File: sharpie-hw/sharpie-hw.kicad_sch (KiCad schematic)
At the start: 0 parts

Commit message: sharpie-hw prototype 1: complete
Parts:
- added H1, H2, H3, H4: MountingHole, symbol Mechanical:MountingHole
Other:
- sheet Power renamed Power_Display
- removed sheet Display

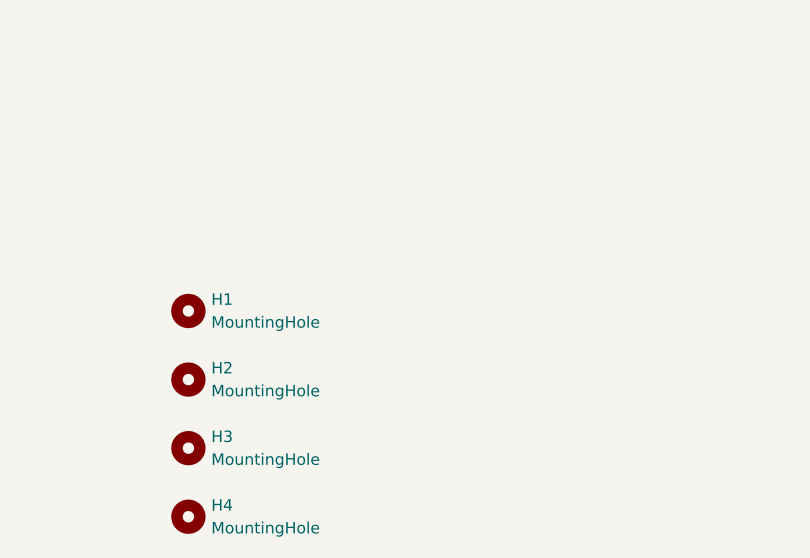
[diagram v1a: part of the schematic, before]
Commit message: Finalize schematic, start PCB, configure manufacturing parameters, and start placing RP2350 components.
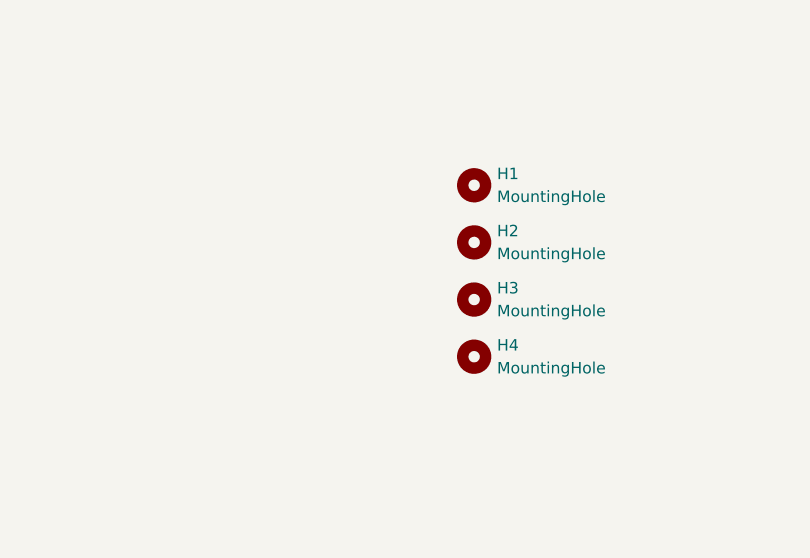
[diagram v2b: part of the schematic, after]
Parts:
- H1, H2, H3, H4: footprint (none) -> MountingHole:MountingHole_3.2mm_M3
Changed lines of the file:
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@@
 	(symbol
 		(lib_id "Mechanical:MountingHole")
-		(at 76.2 132.08 0)
+		(at 107.95 124.46 0)
+		(unit 1)
+		(exclude_from_sim yes)
+		(in_bom no)
+		(on_board yes)
+		(dnp no)
+		(fields_autoplaced yes)
+		(property "Reference" "H2"
+			(at 110.49 123.1899 0)
+			(effects
+				(font
+					(size 1.27 1.27)
+				)
+				(justify left)
+			)
+		)
+		(property "Value" "MountingHole"
+			(at 110.49 125.7299 0)
+			(effects
+				(font
+					(size 1.27 1.27)
+				)
+				(justify left)
+			)
+		)
+		(property "Footprint" "MountingHole:MountingHole_3.2mm_M3"
+			(at 107.95 124.46 0)
+			(effects
+				(font
+					(size 1.27 1.27)
+				)
+				(hide yes)
+			)
+		)
+		(property "Datasheet" "~"
+			(at 107.95 124.46 0)
+			(effects
+				(font
+					(size 1.27 1.27)
+				)
+				(hide yes)
+			)
+		)
+		(property "Description" "Mounting Hole without connection"
+			(at 107.95 124.46 0)
+			(effects
+				(font
+					(size 1.27 1.27)
+				)
+				(hide yes)
+			)
+		)
+		(instances
+			(project "sharpie-hw"
+				(path "/745c0971-f903-4f96-8dfe-3ac35ced6915"
+					(reference "H2")
+					(unit 1)
+				)
+			)
+		)
+	)
+	(symbol
+		(lib_id "Mechanical:MountingHole")
+		(at 107.95 130.81 0)
+		(unit 1)
+		(exclude_from_sim yes)
+		(in_bom no)
+		(on_board yes)
+		(dnp no)
+		(fields_autoplaced yes)
+		(property "Reference" "H3"
+			(at 110.49 129.5399 0)
+			(effects
+				(font
+					(size 1.27 1.27)
+				)
+				(justify left)
+			)
+		)
+		(property "Value" "MountingHole"
+			(at 110.49 132.0799 0)
+			(effects
+				(font
+					(size 1.27 1.27)
+				)
+				(justify left)
+			)
+		)
+		(property "Footprint" "MountingHole:MountingHole_3.2mm_M3"
+			(at 107.95 130.81 0)
+			(effects
+				(font
+					(size 1.27 1.27)
+				)
+				(hide yes)
+			)
+		)
+		(property "Datasheet" "~"
+			(at 107.95 130.81 0)
+			(effects
+				(font
+					(size 1.27 1.27)
+				)
+				(hide yes)
+			)
+		)
+		(property "Description" "Mounting Hole without connection"
+			(at 107.95 130.81 0)
+			(effects
+				(font
+					(size 1.27 1.27)
+				)
+				(hide yes)
+			)
+		)
+		(instances
+			(project ""
+				(path "/745c0971-f903-4f96-8dfe-3ac35ced6915"
+					(reference "H3")
+					(unit 1)
+				)
+			)
+		)
+	)
+	(symbol
+		(lib_id "Mechanical:MountingHole")
+		(at 107.95 118.11 0)
 		(unit 1)
 		(exclude_from_sim yes)
@@
 		(fields_autoplaced yes)
 		(property "Reference" "H1"
-			(at 78.74 130.8099 0)
-			(effects
-				(font
-					(size 1.27 1.27)
-				)
-				(justify left)
-			)
-		)
-		(property "Value" "MountingHole"
-			(at 78.74 133.3499 0)
-			(effects
-				(font
-					(size 1.27 1.27)
-				)
-				(justify left)
-			)
-		)
-		(property "Footprint" ""
-			(at 76.2 132.08 0)
-			(effects
-				(font
-					(size 1.27 1.27)
-				)
-				(hide yes)
-			)
-		)
-		(property "Datasheet" "~"
-			(at 76.2 132.08 0)
-			(effects
-				(font
-					(size 1.27 1.27)
-				)
-				(hide yes)
-			)
-		)
-		(property "Description" "Mounting Hole without connection"
-			(at 76.2 132.08 0)
+			(at 110.49 116.8399 0)
+			(effects
+				(font
+					(size 1.27 1.27)
+				)
+				(justify left)
+			)
+		)
+		(property "Value" "MountingHole"
+			(at 110.49 119.3799 0)
+			(effects
+				(font
+					(size 1.27 1.27)
+				)
+				(justify left)
+			)
+		)
+		(property "Footprint" "MountingHole:MountingHole_3.2mm_M3"
+			(at 107.95 118.11 0)
+			(effects
+				(font
+					(size 1.27 1.27)
+				)
+				(hide yes)
+			)
+		)
+		(property "Datasheet" "~"
+			(at 107.95 118.11 0)
+			(effects
+				(font
+					(size 1.27 1.27)
+				)
+				(hide yes)
+			)
+		)
+		(property "Description" "Mounting Hole without connection"
+			(at 107.95 118.11 0)
 			(effects
 				(font
@@
 	(symbol
 		(lib_id "Mechanical:MountingHole")
-		(at 76.2 147.32 0)
-		(unit 1)
-		(exclude_from_sim yes)
-		(in_bom no)
-		(on_board yes)
-		(dnp no)
-		(fields_autoplaced yes)
-		(property "Reference" "H3"
-			(at 78.74 146.0499 0)
-			(effects
-				(font
-					(size 1.27 1.27)
-				)
-				(justify left)
-			)
-		)
-		(property "Value" "MountingHole"
-			(at 78.74 148.5899 0)
-			(effects
-				(font
-					(size 1.27 1.27)
-				)
-				(justify left)
-			)
-		)
-		(property "Footprint" ""
-			(at 76.2 147.32 0)
-			(effects
-				(font
-					(size 1.27 1.27)
-				)
-				(hide yes)
-			)
-		)
-		(property "Datasheet" "~"
-			(at 76.2 147.32 0)
-			(effects
-				(font
-					(size 1.27 1.27)
-				)
-				(hide yes)
-			)
-		)
-		(property "Description" "Mounting Hole without connection"
-			(at 76.2 147.32 0)
-			(effects
-				(font
-					(size 1.27 1.27)
-				)
-				(hide yes)
-			)
-		)
-		(instances
-			(project ""
-				(path "/745c0971-f903-4f96-8dfe-3ac35ced6915"
-					(reference "H3")
-					(unit 1)
-				)
-			)
-		)
-	)
-	(symbol
-		(lib_id "Mechanical:MountingHole")
-		(at 76.2 139.7 0)
-		(unit 1)
-		(exclude_from_sim yes)
-		(in_bom no)
-		(on_board yes)
-		(dnp no)
-		(fields_autoplaced yes)
-		(property "Reference" "H2"
-			(at 78.74 138.4299 0)
-			(effects
-				(font
-					(size 1.27 1.27)
-				)
-				(justify left)
-			)
-		)
-		(property "Value" "MountingHole"
-			(at 78.74 140.9699 0)
-			(effects
-				(font
-					(size 1.27 1.27)
-				)
-				(justify left)
-			)
-		)
-		(property "Footprint" ""
-			(at 76.2 139.7 0)
-			(effects
-				(font
-					(size 1.27 1.27)
-				)
-				(hide yes)
-			)
-		)
-		(property "Datasheet" "~"
-			(at 76.2 139.7 0)
-			(effects
-				(font
-					(size 1.27 1.27)
-				)
-				(hide yes)
-			)
-		)
-		(property "Description" "Mounting Hole without connection"
-			(at 76.2 139.7 0)
-			(effects
-				(font
-					(size 1.27 1.27)
-				)
-				(hide yes)
-			)
-		)
-		(instances
-			(project ""
-				(path "/745c0971-f903-4f96-8dfe-3ac35ced6915"
-					(reference "H2")
-					(unit 1)
-				)
-			)
-		)
-	)
-	(symbol
-		(lib_id "Mechanical:MountingHole")
-		(at 76.2 154.94 0)
+		(at 107.95 137.16 0)
 		(unit 1)
 		(exclude_from_sim yes)
@@
 		(fields_autoplaced yes)
 		(property "Reference" "H4"
-			(at 78.74 153.6699 0)
-			(effects
-				(font
-					(size 1.27 1.27)
-				)
-				(justify left)
-			)
-		)
-		(property "Value" "MountingHole"
-			(at 78.74 156.2099 0)
-			(effects
-				(font
-					(size 1.27 1.27)
-				)
-				(justify left)
-			)
-		)
-		(property "Footprint" ""
-			(at 76.2 154.94 0)
-			(effects
-				(font
-					(size 1.27 1.27)
-				)
-				(hide yes)
-			)
-		)
-		(property "Datasheet" "~"
-			(at 76.2 154.94 0)
-			(effects
-				(font
-					(size 1.27 1.27)
-				)
-				(hide yes)
-			)
-		)
-		(property "Description" "Mounting Hole without connection"
-			(at 76.2 154.94 0)
-			(effects
-				(font
+			(at 110.49 135.8899 0)
+			(effects
+				(font
+					(size 1.27 1.27)
+				)
+				(justify left)
+			)
+		)
+		(property "Value" "MountingHole"
+			(at 110.49 138.4299 0)
+			(effects
+				(font
+					(size 1.27 1.27)
+				)
+				(justify left)
+			)
+		)
+		(property "Footprint" "MountingHole:MountingHole_3.2mm_M3"
+			(at 107.95 137.16 0)
+			(effects
+				(font
+					(size 1.27 1.27)
+				)
+				(hide yes)
+			)
+		)
+		(property "Datasheet" "~"
+			(at 107.95 137.16 0)
+			(effects
+				(font
+					(size 1.27 1.27)
+				)
+				(hide yes)
+			)
+		)
+		(property "Description" "Mounting Hole without connection"
+			(at 107.95 137.16 0)
+			(effects
+				(font
